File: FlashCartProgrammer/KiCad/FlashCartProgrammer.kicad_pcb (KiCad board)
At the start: 2 copper layers, 100 x 100 mm, 85 parts, among them J1 Vic20 Cartridge Connector, J10 Vic20 Header, J11 ZIF Header, J2 C64 Cartridge Connector, J3 +5V, J4 USB_A_KeyBoard, J5 BOOT SEL, J6 VGA, J7 DM3D-SF, J8 SWD, J9 C64 Header, U1 TLV74311PDBVR, U10 27C400, U2 TLV74333PDBVR, U3 W25Q16JVSSIQ, U4 RP2350B-QFN80, U5 74LS573, U6 74LS573, U7 TXS0108EPW, U8 TXS0108EPW, U9 TXS0108EPW, Y1 12MHz

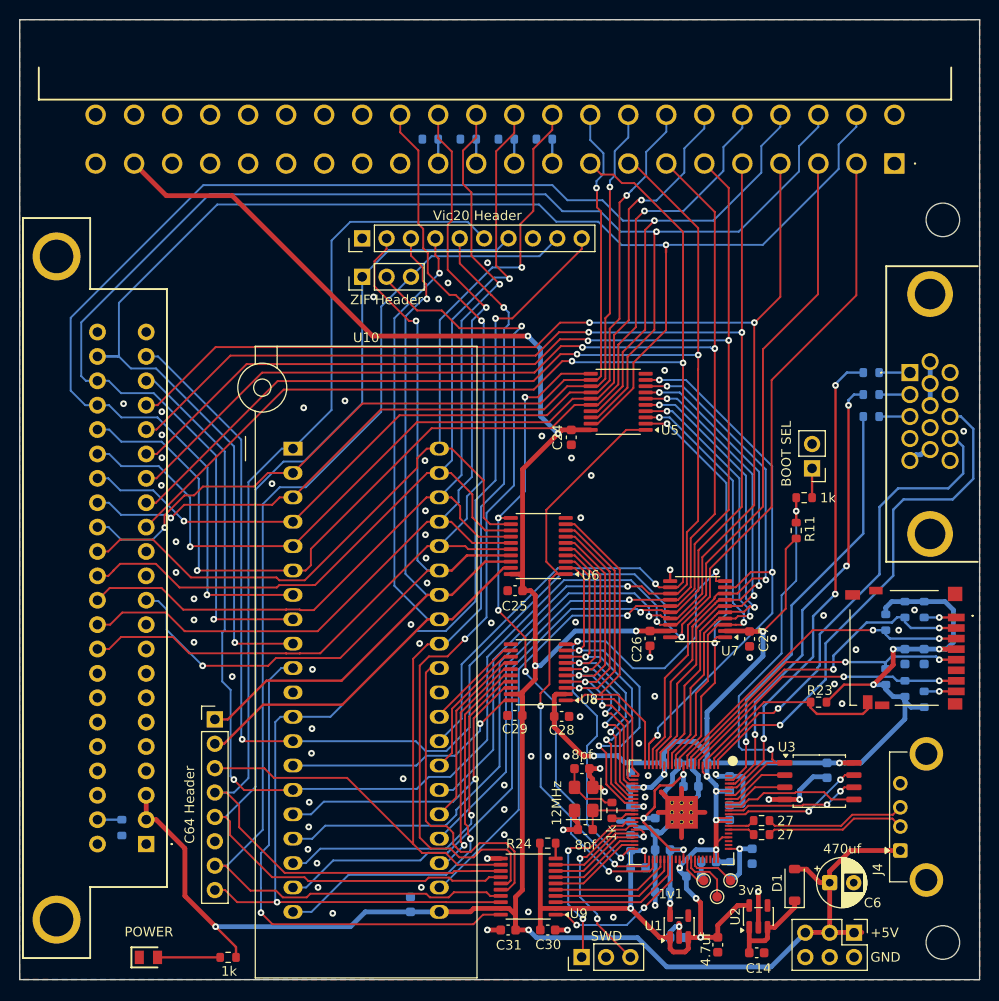
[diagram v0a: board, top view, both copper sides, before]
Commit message: - Cleaned up the Flash Cart Programmer PCB a bit.
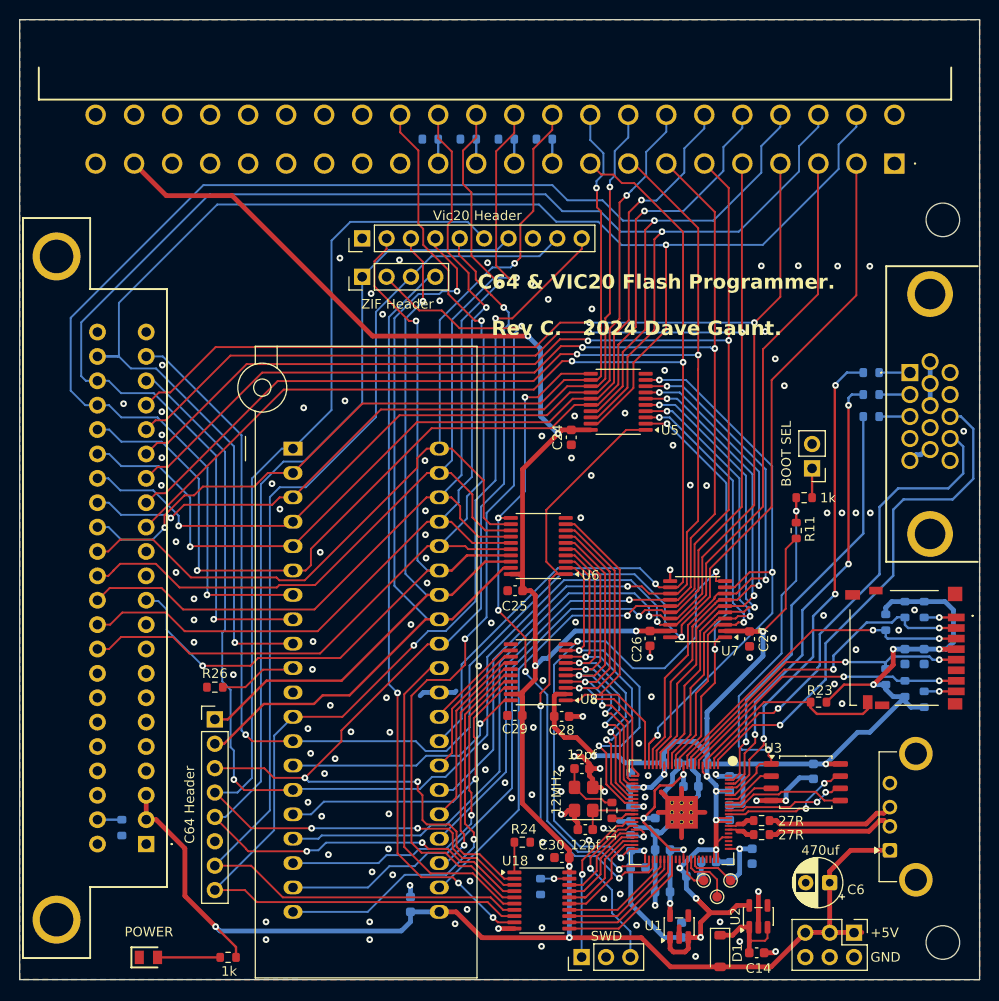
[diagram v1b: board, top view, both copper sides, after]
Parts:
- removed C15: 4.7uf, Capacitor_SMD:C_0603_1608Metric
- removed C31: 100nf, Capacitor_SMD:C_0603_1608Metric
- removed U9: TXS0108EPW, Package_SO:TSSOP-20_4.4x6.5mm_P0.65mm
- added R25: 10k, Resistor_SMD:R_0603_1608Metric, B.Cu at (149.1, 139.0)
- added R26: 10k, Resistor_SMD:R_0603_1608Metric, F.Cu at (115.1, 118.3)
- added U18: 74LS245, Package_SO:TSSOP-20_4.4x6.5mm_P0.65mm, F.Cu at (149.2, 140.5)
- C22, C23: value 8pf -> 12pf
- J1: value Vic20 Cartridge Connector -> Vic20_Cartridge_Connector; footprint SamacSys_Parts:307044558201 -> _Custom:Vic20-Cartridge-Connector
- J11: footprint Connector_PinHeader_2.54mm:PinHeader_1x03_P2.54mm_Vertical -> Connector_PinHeader_2.54mm:PinHeader_1x04_P2.54mm_Vertical
- J2: value C64 Cartridge Connector -> c64-Cartridge-Connector; footprint SamacSys_Parts:395044524202 -> _Custom:c64-Cartridge-Connector
- J4: footprint Connector_USB:USB_A_Connfly_DS1095 -> _Custom:USB_A
- J6: value VGA -> DE15_Socket_HighDensity_MountingHoles; footprint SamacSys_Parts:117345301 -> _Custom:DSUB-15
- R1, R2, R3, R4, R5, R7, R8, R9: value 27 -> 27R
- R10, R12, R14: value 340 -> 330R
- U10: footprint Socket:DIP_Socket-40_W11.9mm_W12.7mm_W15.24mm_W17.78mm_W18.5mm_3M_240-1280-00-0602J -> _Custom:ZIF-40_W11.9_W12.7_W15.24_W17.78_W18.5_3M_240-1280-00-0602J
- moved D1 10.4 mm to (167.8, 145.7), turned to -90 degrees
- moved C30 7.69 mm to (151.3, 136.0), turned to 0 degrees
- moved R24 2.65 mm to (147.2, 134.4), turned to 0 degrees
- moved U3 1.42 mm to (176.7, 128.2)
- moved C19 1.42 mm to (177.5, 127.0)
- moved J4 1.09 mm to (185.4, 135.2)
- moved C1 0.89 mm to (163.7, 143.6), turned to -90 degrees
- turned C6 to 180 degrees
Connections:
- net /SPI1.CS renamed /SPI1.~{CS}
- C30 pad 2: +3V3 -> +5V
- R24 pad 2: +3V3 -> GND
- U10 pad 10: ~{CE} -> Net-(U10-~{CE})
- U4 pad 48: /~{3v3_CE} -> /~{3v3_RESET}
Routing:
- net ~{RESET}: track 0.00 -> 78.0 mm, vias 0 -> 3
- net ~{CE}: track 53.5 -> 0.00 mm, vias 1 -> 0
- net +3V3: track 217.3 -> 198.5 mm, vias 18 -> 17
- net /~{3v3_CE}: track 16.6 -> 0.00 mm, vias 2 -> 0
- net /~{3v3_RESET}: track 0.00 -> 14.7 mm
- net Net-(U10-~{CE}): track 0.00 -> 8.14 mm
- net GND: track 92.7 -> 98.5 mm, vias 81 -> 130
- net /A15: track 82.9 -> 86.6 mm
- net Net-(U18-CE): track 0.00 -> 3.00 mm, vias 0 -> 1
- net /A16: track 104.3 -> 107.2 mm, vias 1 -> 3
- net /2350_SWCLK: track 20.0 -> 17.2 mm, vias 2 -> 1
- net /2350_QSPI.~{CS}: track 43.7 -> 41.1 mm
- net 3v3_DATA_OE: track 53.3 -> 55.9 mm
- net ~{OE}: track 118.6 -> 121.2 mm
- net +5V: track 252.4 -> 250.1 mm, vias 6 -> 7
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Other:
- board text added: "C64 & VIC20 Flash Programmer. Rev C. 2024 Dave Gaunt."
- board text removed: "C64 & VIC20 Flash Programmer. Rev B. 2024 Dave Gaunt."

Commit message: - Removed references to my local parts.
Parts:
- C22, C23: value 12pf -> 10pf
- J7: footprint SamacSys_Parts:DM3DSF -> _Custom:DM3DSF_SDCard
- Power1: footprint SamacSys_Parts:LEDC2012X90N -> LED_SMD:LED_0805_2012Metric
- R13: value 1k -> 2k2
- U3: footprint Dave Footprints:SOIC-8_5.23x5.23mm_P1.27mm -> Package_SO:SOIC-8_5.3x5.3mm_P1.27mm
- U4: value RP2350B-QFN80 -> RP2354B-QFN80
